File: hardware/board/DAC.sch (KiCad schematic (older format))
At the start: 5 parts, among them U6 AD5685R?RUZ

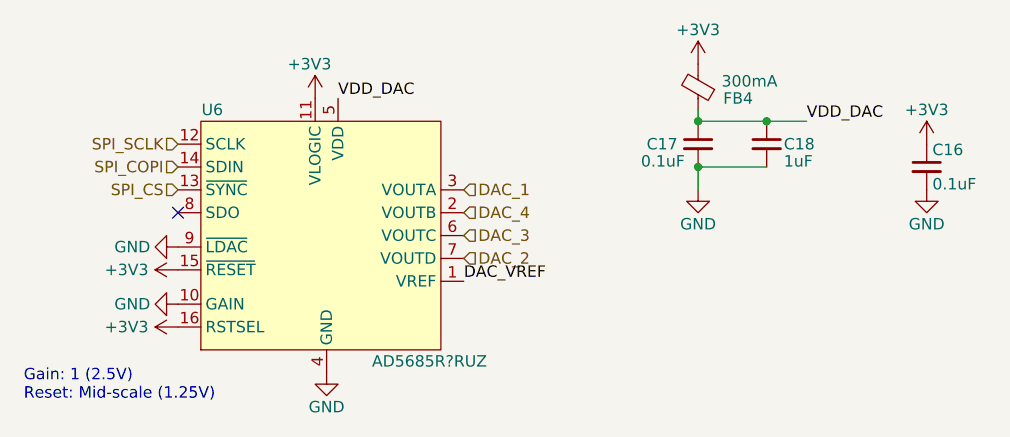
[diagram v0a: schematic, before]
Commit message: Fix issues found in hardware v1
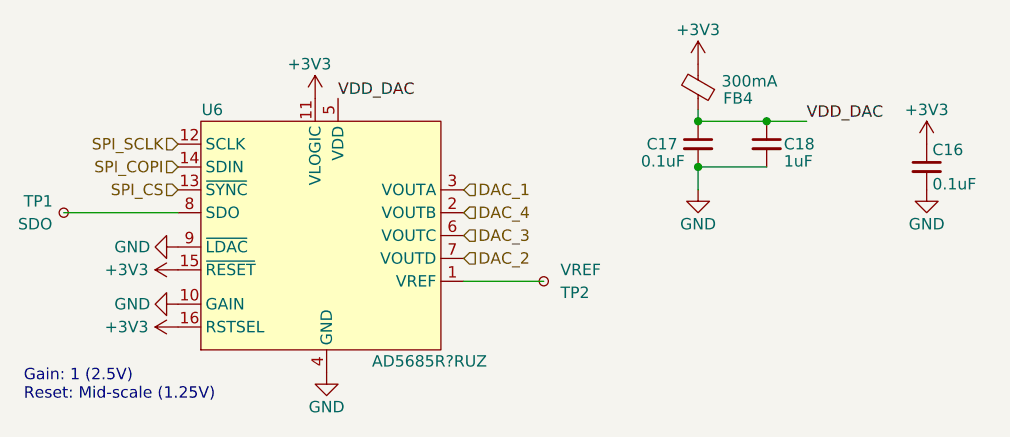
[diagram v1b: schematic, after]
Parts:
- added TP1: SDO, TestPoint:TestPoint_Pad_D1.0mm, symbol Connector:TestPoint_Small
- added TP2: VREF, TestPoint:TestPoint_Pad_D1.0mm, symbol Connector:TestPoint_Small
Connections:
- net at U6.8 (SDO): now also TP1.1
- net DAC_VREF: no longer names the net of U6.1 (VREF)
- net DAC_VREF: now also TP2.1
- no-connect marks 1 -> 0
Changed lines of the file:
@@
 Sheet 6 7
 Title "TestKit Motherboard"
-Date "2021-10-22"
-Rev "v1"
+Date "2021-11-12"
+Rev "v2"
 Comp "Winterbloom"
 Comment1 "Alethea Flowers"
@@
 	1    0    0    -1
 $EndComp
-NoConn ~ 1850 2675
 $Comp
 L power:GND #PWR?
@@
 Text Label 2550 2175 0    50   ~ 0
 VDD_DAC
-Text Label 3100 2975 0    50   ~ 0
-DAC_VREF
 Text HLabel 3100 2575 2    50   Input ~ 0
 DAC_1
@@
 Text Notes 1175 3500 0    50   ~ 0
 Gain: 1 (2.5V)\nReset: Mid-scale (1.25V)
+$Comp
+L Connector:TestPoint_Small TP1
+U 1 1 618096C4
+P 1350 2675
+F 0 "TP1" H 1525 2625 50  0000 R CNN
+F 1 "SDO" H 1550 2725 50  0000 R CNN
+F 2 "TestPoint:TestPoint_Pad_D1.0mm" H 1550 2675 50  0001 C CNN
+F 3 "~" H 1550 2675 50  0001 C CNN
+	1    1350 2675
+	-1   0    0    1
+$EndComp
+Wire Wire Line
+	1850 2675 1350 2675
+$Comp
+L Connector:TestPoint_Small TP2
+U 1 1 6180BA3F
+P 3450 2975
+F 0 "TP2" H 3650 2925 50  0000 R CNN
+F 1 "VREF" H 3700 3025 50  0000 R CNN
+F 2 "TestPoint:TestPoint_Pad_D1.0mm" H 3650 2975 50  0001 C CNN
+F 3 "~" H 3650 2975 50  0001 C CNN
+	1    3450 2975
+	1    0    0    -1
+$EndComp
+Wire Wire Line
+	3450 2975 3100 2975
 $EndSCHEMATC
